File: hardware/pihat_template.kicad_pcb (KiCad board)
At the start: 2 copper layers, 65 x 56.5 mm, 37 parts, among them P1 CONN_01X02, P2 CONN_01X02, P3 Raspberry_Pi_+_Conn, Q1 BSS138, U1 LM3489, U2 CAT24C32HU4I-GT3, U3 FDC5614P, U4 LM1117IMPX-ADJ, U5 DMMT5401

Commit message: created DMMT5401 footprint and updated netlist
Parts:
- C2, C3, C4, C5, C7, C8: footprint project:c_0402 -> project:c_0805
- JP1: footprint w_smd_resistors:r_0603 -> project:r_0805
- P3: footprint project:pin_socket_20x2_mirrored -> project:pin_socket_20x2
- R1, R10, R11, R12, R2, R3, R4, R5, R6, R7, R8, R9: footprint project:r_0402 -> project:r_0805
- U2: value CAT24C32HU4I-GT3 -> CAT24C04WI-GT3; footprint project:tssop-8 -> project:CAT24C04WI-GT3
- moved D3 37.5 mm to (108.7, 119.4), turned to 180 degrees
- moved R10 36.8 mm to (117.1, 114.8)
- moved U5 4.16 mm to (111.0, 80.5)
- moved R12 3.88 mm to (107.7, 83.8)
- moved Q1 3.57 mm to (107.4, 80.5)
- moved R11 2.58 mm to (111.8, 83.8)
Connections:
- net +3V3 renamed +3.3V
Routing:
- net +3.3V: track 178.7 -> 0.00 mm, vias 6 -> 0
- net +5V: track 114.3 -> 0.00 mm, vias 2 -> 0
- net GND: track 51.0 -> 0.00 mm, vias 13 -> 0
- net Net-(P3-Pad27): track 36.5 -> 0.00 mm, vias 1 -> 0
- net +24V: track 35.0 -> 0.00 mm
- net Net-(P3-Pad28): track 32.9 -> 0.00 mm
- net /Back Power Protection/5V_MCU: track 15.5 -> 0.00 mm
- net Net-(JP1-Pad1): track 11.5 -> 0.00 mm, vias 1 -> 0
- net Net-(Q1-Pad1): track 8.73 -> 0.00 mm
- net Net-(U1-Pad7): track 5.38 -> 0.00 mm
- net Net-(C5-Pad2): track 5.06 -> 0.00 mm
- net Net-(R11-Pad1): track 3.43 -> 0.00 mm
- net Net-(R8-Pad1): track 2.87 -> 0.00 mm
- net Net-(C3-Pad2): track 2.74 -> 0.00 mm
- net Net-(R4-Pad2): track 1.26 -> 0.00 mm
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
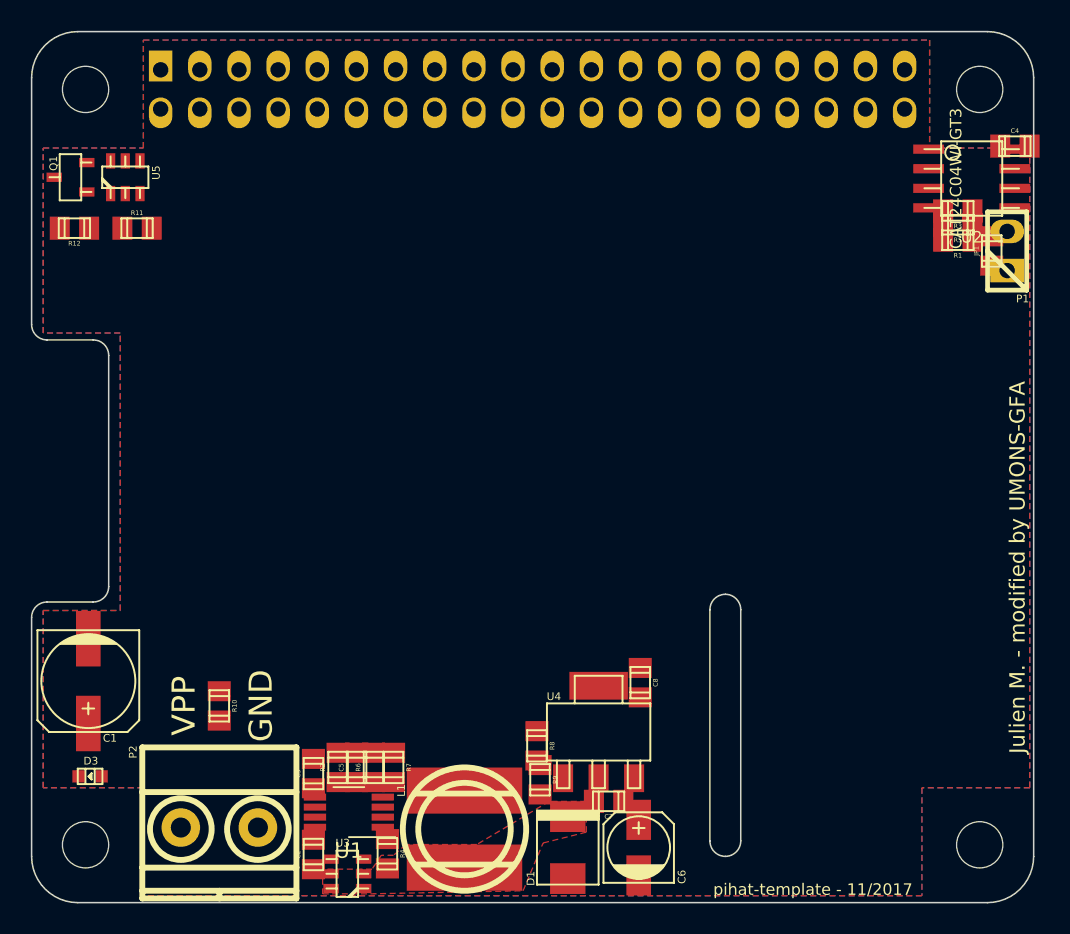
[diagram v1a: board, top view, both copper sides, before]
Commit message: refactored pihat to include larger components, reorganize space around tiny components and let spaces along edges for further connectors, battery holder...
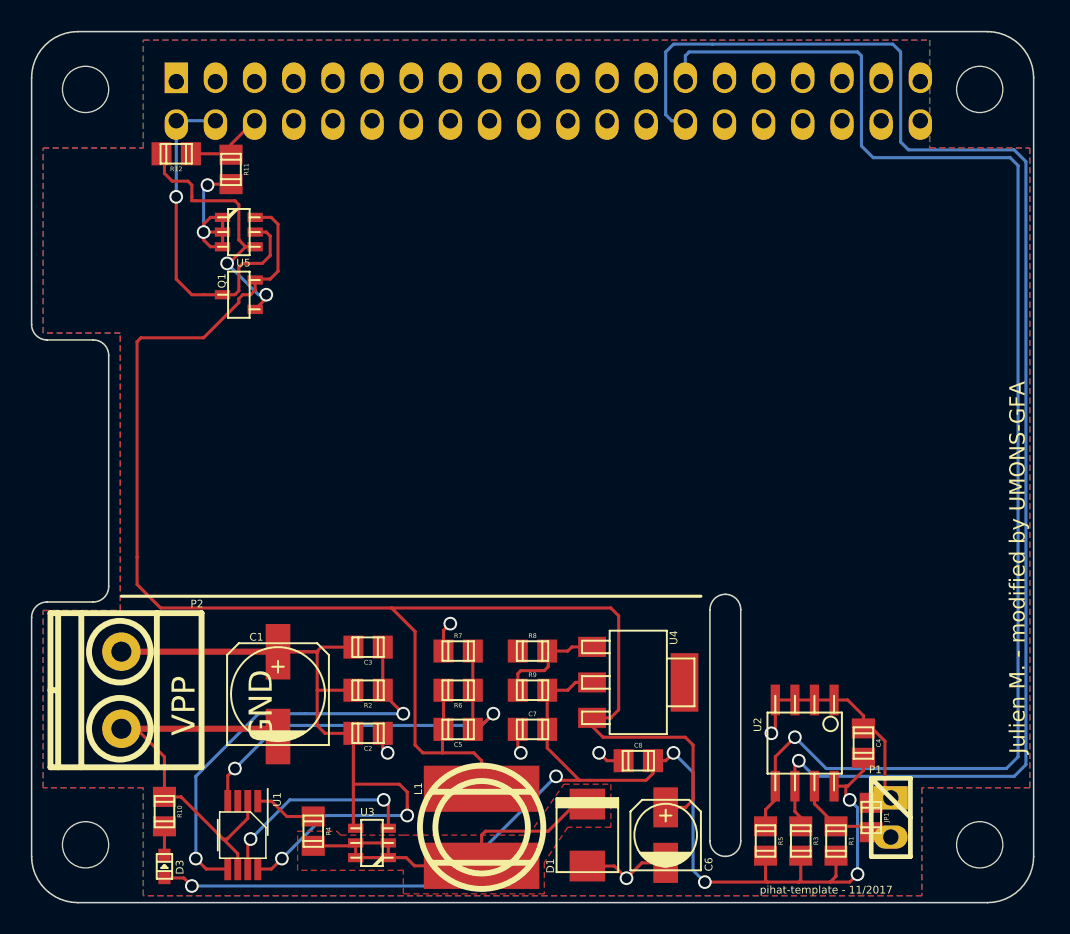
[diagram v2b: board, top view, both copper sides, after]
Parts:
- U1: footprint project:VSSOP-8_3.0x3.0mm_Pitch0.65mm -> project:LM3489
- moved R3 42.1 mm to (154.8, 123.6), turned to 270 degrees
- moved R5 41.9 mm to (152.5, 123.6), turned to 270 degrees
- moved C4 39.9 mm to (158.9, 117.2), turned to 270 degrees
- moved R1 39.8 mm to (157.1, 123.6), turned to 270 degrees
- moved U2 38.2 mm to (155.1, 117.2), turned to 180 degrees
- moved JP1 37.6 mm to (159.4, 122.0), turned to 270 degrees
- moved P1 37.5 mm to (160.7, 122.0), turned to 270 degrees
- moved Q1 13.3 mm to (118.4, 88.1)
- moved C1 12.3 mm to (120.9, 114.0), turned to 90 degrees
- moved P2 10.9 mm to (110.7, 113.8), turned to 270 degrees
- moved C3 8.94 mm to (126.7, 111.0), turned to 180 degrees
- moved R7 8.63 mm to (132.6, 111.3), turned to 0 degrees
- moved C2 8.63 mm to (126.7, 116.6), turned to 180 degrees
- moved U5 8.18 mm to (118.4, 84.1), turned to 270 degrees
- moved R12 8.18 mm to (114.3, 79.0)
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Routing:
- net +5V: track 0.00 -> 132.9 mm
- net Net-(P3-Pad28): track 0.00 -> 95.4 mm, vias 0 -> 1
- net Net-(P3-Pad27): track 0.00 -> 90.4 mm, vias 0 -> 1
- net +3.3V: track 0.00 -> 81.3 mm, vias 0 -> 6
- net GND: track 0.00 -> 62.4 mm, vias 0 -> 6
- net +24V: track 0.00 -> 50.9 mm, vias 0 -> 2
- net Net-(C3-Pad2): track 0.00 -> 27.7 mm, vias 0 -> 2
- net Net-(C5-Pad2): track 0.00 -> 27.4 mm, vias 0 -> 2
- net Net-(D1-Pad2): track 0.00 -> 24.9 mm
- net /Back Power Protection/5V_MCU: track 0.00 -> 23.6 mm, vias 0 -> 1
- net Net-(Q1-Pad1): track 0.00 -> 17.9 mm, vias 0 -> 2
- net Net-(U1-Pad7): track 0.00 -> 13.7 mm, vias 0 -> 2
- net Net-(R11-Pad1): track 0.00 -> 11.7 mm, vias 0 -> 2
- net Net-(R8-Pad1): track 0.00 -> 7.29 mm
- net Net-(JP1-Pad1): track 0.00 -> 7.03 mm
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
